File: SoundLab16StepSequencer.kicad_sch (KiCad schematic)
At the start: 8 parts, among them J1 External Start, J2 External Clock Input, J3 Trigger Out, J4 Gate Out, J5 External Clock Output, J6 Sequencer CV3, J7 Sequencer CV2, J8 Sequencer CV1

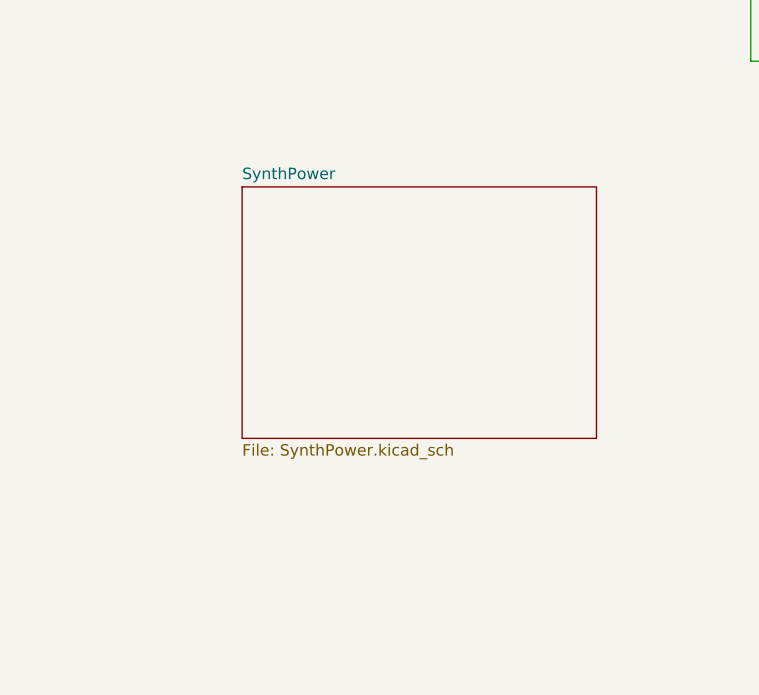
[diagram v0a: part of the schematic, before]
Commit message: created pcb file, placed parts
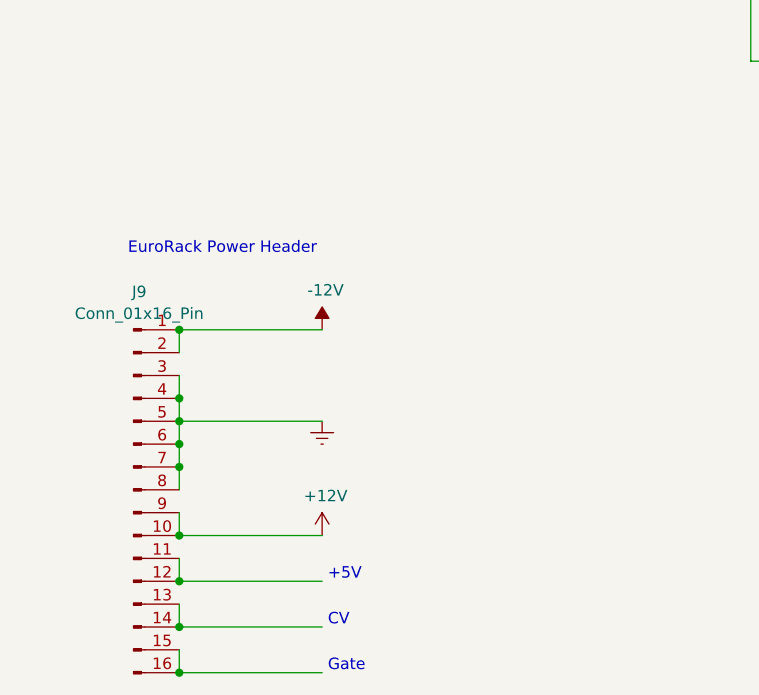
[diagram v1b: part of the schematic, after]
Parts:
- added J9: Conn_01x16_Pin, Connector_PinHeader_2.54mm:PinHeader_2x08_P2.54mm_Vertical, symbol Connector:Conn_01x16_Pin
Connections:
- net GNDREF: now also J9.3 (Pin_3), J9.4 (Pin_4), J9.5 (Pin_5), J9.6 (Pin_6), J9.7 (Pin_7), J9.8 (Pin_8)
- new net: J9.11 (Pin_11), J9.12 (Pin_12)
- new net: J9.13 (Pin_13), J9.14 (Pin_14)
- new net: J9.15 (Pin_15), J9.16 (Pin_16)
- new net +12V: J9.10 (Pin_10), J9.9 (Pin_9)
- new net -12V: J9.1 (Pin_1), J9.2 (Pin_2)
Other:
- removed sheet SynthPower
- note added: "+5V"
- note added: "CV"
- note added: "EuroRack Power Header"
- note added: "Gate"

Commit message: routing and placing
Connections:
- net XCLK renamed VariClock2/Clock_Out
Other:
- sheet SequencerClocking ports: added none; removed CKOUT, XCLK
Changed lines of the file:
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@@
   (junction (at 144.78 52.705) (diameter 0) (color 0 0 0 0)
   )
-  (junction (at 215.9 113.665) (diameter 0) (color 0 0 0 0)
-  )
   (junction (at 139.7 79.375) (diameter 0) (color 0 0 0 0)
   )
@@
     (stroke (width 0) (type default))
   )
-  (wire (pts (xy 215.9 102.87) (xy 220.345 102.87))
-    (stroke (width 0) (type default))
-  )
   (wire (pts (xy 114.3 94.615) (xy 147.32 94.615))
     (stroke (width 0) (type default))
@@
     (stroke (width 0) (type default))
   )
-  (wire (pts (xy 215.9 113.665) (xy 215.9 102.87))
-    (stroke (width 0) (type default))
-  )
   (wire (pts (xy 124.46 70.485) (xy 124.46 84.455))
     (stroke (width 0) (type default))
@@
     (stroke (width 0) (type default))
   )
-  (wire (pts (xy 224.79 113.665) (xy 215.9 113.665))
-    (stroke (width 0) (type default))
-  )
   (wire (pts (xy 121.92 73.025) (xy 121.92 86.995))
     (stroke (width 0) (type default))
   )
-  (wire (pts (xy 55.245 62.865) (xy 55.245 69.215))
-    (stroke (width 0) (type default))
-  )
   (wire (pts (xy 178.435 119.38) (xy 187.325 119.38))
     (stroke (width 0) (type default))
@@
     (stroke (width 0) (type default))
   )
-  (wire (pts (xy 215.9 113.665) (xy 213.36 113.665))
+  (wire (pts (xy 213.36 113.665) (xy 224.79 113.665))
     (stroke (width 0) (type default))
   )
@@
   )
   (wire (pts (xy 99.06 46.99) (xy 106.68 46.99))
-    (stroke (width 0) (type default))
-  )
-  (wire (pts (xy 55.245 69.215) (xy 67.31 69.215))
     (stroke (width 0) (type default))
   )
@@
   )
   (text "+5V" (at 59.69 171.45 0)
-    (effects (font (size 1.27 1.27)) (justify left bottom))
-  )
-  (label "XCLK" (at 220.345 102.87 0) (fields_autoplaced)
-    (effects (font (size 1.27 1.27)) (justify left bottom))
-  )
-  (label "XCLK" (at 55.245 62.865 0) (fields_autoplaced)
     (effects (font (size 1.27 1.27)) (justify left bottom))
   )
@@
       (effects (font (size 1.27 1.27)) (justify right))
     )
-    (pin "CKOUT" output (at 99.06 65.405 0)
-      (effects (font (size 1.27 1.27)) (justify right))
-    )
     (pin "QD" output (at 99.06 60.325 0)
       (effects (font (size 1.27 1.27)) (justify right))
@@
       (effects (font (size 1.27 1.27)) (justify right))
     )
-    (pin "XCLK" input (at 67.31 69.215 180)
-      (effects (font (size 1.27 1.27)) (justify left))
-    )
     (pin "STP" output (at 99.06 80.645 0)

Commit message: added manufacturing files for v1
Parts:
- added H1, H2, H3, H4: MountingHole, MountingHole:MountingHole_4.3mm_M4_Pad, symbol Mechanical:MountingHole
- J1, J2, J3, J4, J5, J6, J7, J8: footprint SynthProjConnectors:PJ-301 -> SynthProjConnectors:PJ-301-BM
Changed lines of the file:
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@@
     (effects (font (size 1.27 1.27)) (justify left bottom))
   )
+  (symbol (lib_id "Mechanical:MountingHole") (at 229.87 132.715 0) (unit 1)
+    (in_bom yes) (on_board yes) (dnp no) (fields_autoplaced)
+    (property "Reference" "H3" (at 232.41 131.445 0)
+      (effects (font (size 1.27 1.27)) (justify left))
+    )
+    (property "Value" "MountingHole" (at 232.41 133.985 0)
+      (effects (font (size 1.27 1.27)) (justify left))
+    )
+    (property "Footprint" "MountingHole:MountingHole_4.3mm_M4_Pad" (at 229.87 132.715 0)
+      (effects (font (size 1.27 1.27)) hide)
+    )
+    (property "Datasheet" "~" (at 229.87 132.715 0)
+      (effects (font (size 1.27 1.27)) hide)
+    )
+    (instances
+      (project "SoundLab16StepSequencer"
+        (path "/0a1377c9-61ff-44bc-b9df-99baf54c0c4b"
+          (reference "H3") (unit 1)
+        )
+      )
+    )
+  )
   (symbol (lib_id "SynthProj-rescue:AudioJack2-Connector") (at 248.92 54.61 0) (mirror y) (unit 1)
     (in_bom yes) (on_board yes) (dnp no)
@@
       (effects (font (size 1.27 1.27)))
     )
-    (property "Footprint" "SynthProjConnectors:PJ-301" (at 248.92 54.61 0)
+    (property "Footprint" "SynthProjConnectors:PJ-301-BM" (at 248.92 54.61 0)
       (effects (font (size 1.27 1.27)) hide)
     )
@@
       (effects (font (size 1.27 1.27)))
     )
-    (property "Footprint" "SynthProjConnectors:PJ-301" (at 187.96 74.295 0)
+    (property "Footprint" "SynthProjConnectors:PJ-301-BM" (at 187.96 74.295 0)
       (effects (font (size 1.27 1.27)) hide)
     )
@@
       (effects (font (size 1.27 1.27)))
     )
-    (property "Footprint" "SynthProjConnectors:PJ-301" (at 165.1 128.27 0)
+    (property "Footprint" "SynthProjConnectors:PJ-301-BM" (at 165.1 128.27 0)
       (effects (font (size 1.27 1.27)) hide)
     )
@@
     )
   )
+  (symbol (lib_id "Mechanical:MountingHole") (at 229.87 137.795 0) (unit 1)
+    (in_bom yes) (on_board yes) (dnp no) (fields_autoplaced)
+    (property "Reference" "H4" (at 232.41 136.525 0)
+      (effects (font (size 1.27 1.27)) (justify left))
+    )
+    (property "Value" "MountingHole" (at 232.41 139.065 0)
+      (effects (font (size 1.27 1.27)) (justify left))
+    )
+    (property "Footprint" "MountingHole:MountingHole_4.3mm_M4_Pad" (at 229.87 137.795 0)
+      (effects (font (size 1.27 1.27)) hide)
+    )
+    (property "Datasheet" "~" (at 229.87 137.795 0)
+      (effects (font (size 1.27 1.27)) hide)
+    )
+    (instances
+      (project "SoundLab16StepSequencer"
+        (path "/0a1377c9-61ff-44bc-b9df-99baf54c0c4b"
+          (reference "H4") (unit 1)
+        )
+      )
+    )
+  )
   (symbol (lib_id "SynthProj-rescue:AudioJack2-Connector") (at 33.02 51.435 0) (unit 1)
     (in_bom yes) (on_board yes) (dnp no)
@@
       (effects (font (size 1.27 1.27)))
     )
-    (property "Footprint" "SynthProjConnectors:PJ-301" (at 33.02 51.435 0)
+    (property "Footprint" "SynthProjConnectors:PJ-301-BM" (at 33.02 51.435 0)
       (effects (font (size 1.27 1.27)) hide)
     )
@@
       (effects (font (size 1.27 1.27)))
     )
-    (property "Footprint" "SynthProjConnectors:PJ-301" (at 248.285 41.91 0)
+    (property "Footprint" "SynthProjConnectors:PJ-301-BM" (at 248.285 41.91 0)
       (effects (font (size 1.27 1.27)) hide)
     )
@@
       (effects (font (size 1.27 1.27)))
     )
-    (property "Footprint" "SynthProjConnectors:PJ-301" (at 229.87 113.665 0)
+    (property "Footprint" "SynthProjConnectors:PJ-301-BM" (at 229.87 113.665 0)
       (effects (font (size 1.27 1.27)) hide)
     )
@@
     )
   )
+  (symbol (lib_id "Mechanical:MountingHole") (at 229.87 122.555 0) (unit 1)
+    (in_bom yes) (on_board yes) (dnp no) (fields_autoplaced)
+    (property "Reference" "H1" (at 232.41 121.285 0)
+      (effects (font (size 1.27 1.27)) (justify left))
+    )
+    (property "Value" "MountingHole" (at 232.41 123.825 0)
+      (effects (font (size 1.27 1.27)) (justify left))
+    )
+    (property "Footprint" "MountingHole:MountingHole_4.3mm_M4_Pad" (at 229.87 122.555 0)
+      (effects (font (size 1.27 1.27)) hide)
+    )
+    (property "Datasheet" "~" (at 229.87 122.555 0)
+      (effects (font (size 1.27 1.27)) hide)
+    )
+    (instances
+      (project "SoundLab16StepSequencer"
+        (path "/0a1377c9-61ff-44bc-b9df-99baf54c0c4b"
+          (reference "H1") (unit 1)
+        )
+      )
+    )
+  )
   (symbol (lib_id "SynthProj-rescue:AudioJack2-Connector") (at 187.96 83.185 0) (mirror y) (unit 1)
     (in_bom yes) (on_board yes) (dnp no)
@@
       (effects (font (size 1.27 1.27)))
     )
-    (property "Footprint" "SynthProjConnectors:PJ-301" (at 187.96 83.185 0)
+    (property "Footprint" "SynthProjConnectors:PJ-301-BM" (at 187.96 83.185 0)
       (effects (font (size 1.27 1.27)) hide)
     )
@@
     )
   )
+  (symbol (lib_id "Mechanical:MountingHole") (at 229.87 127.635 0) (unit 1)
+    (in_bom yes) (on_board yes) (dnp no) (fields_autoplaced)
+    (property "Reference" "H2" (at 232.41 126.365 0)
+      (effects (font (size 1.27 1.27)) (justify left))
+    )
+    (property "Value" "MountingHole" (at 232.41 128.905 0)
+      (effects (font (size 1.27 1.27)) (justify left))
+    )
+    (property "Footprint" "MountingHole:MountingHole_4.3mm_M4_Pad" (at 229.87 127.635 0)
+      (effects (font (size 1.27 1.27)) hide)
+    )
+    (property "Datasheet" "~" (at 229.87 127.635 0)
+      (effects (font (size 1.27 1.27)) hide)
+    )
+    (instances
+      (project "SoundLab16StepSequencer"
+        (path "/0a1377c9-61ff-44bc-b9df-99baf54c0c4b"
+          (reference "H2") (unit 1)
+        )
+      )
+    )
+  )
   (symbol (lib_id "power:GNDREF") (at 182.88 71.755 0) (unit 1)
     (in_bom yes) (on_board yes) (dnp no)
@@
       (effects (font (size 1.27 1.27)))
     )
-    (property "Footprint" "SynthProjConnectors:PJ-301" (at 248.92 67.31 0)
-      (effects (font (size 1.27 1.27)) hide)
-    )
+    (property "Footprint" "SynthProjConnectors:PJ-301-BM" (at 248.92 67.31 0)
+      (effects (font (size 1.27 1.27)) hide)
+    )

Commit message: lots of work... created faceplate
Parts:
- added H5: MountingHole, MountingHole:MountingHole_4.3mm_M4_Pad, symbol Mechanical:MountingHole
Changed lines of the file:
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@@
+    )
+  )
+  (symbol (lib_id "Mechanical:MountingHole") (at 229.87 143.51 0) (unit 1)
+    (in_bom yes) (on_board yes) (dnp no) (fields_autoplaced)
+    (property "Reference" "H5" (at 232.41 142.24 0)
+      (effects (font (size 1.27 1.27)) (justify left))
+    )
+    (property "Value" "MountingHole" (at 232.41 144.78 0)
+      (effects (font (size 1.27 1.27)) (justify left))
+    )
+    (property "Footprint" "MountingHole:MountingHole_4.3mm_M4_Pad" (at 229.87 143.51 0)
+      (effects (font (size 1.27 1.27)) hide)
+    )
+    (property "Datasheet" "~" (at 229.87 143.51 0)
+      (effects (font (size 1.27 1.27)) hide)
+    )
+    (instances
+      (project "SoundLab16StepSequencer"
+        (path "/0a1377c9-61ff-44bc-b9df-99baf54c0c4b"
+          (reference "H5") (unit 1)
+        )
+      )
     )
   )
